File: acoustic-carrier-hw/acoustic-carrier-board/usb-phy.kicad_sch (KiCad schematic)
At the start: 59 parts, among them IC1 ECP5-BGA256, J9 TYPE-C-31-M-12, U18 LMV321, U6 TS3USB30EDGSR, U7 USB3300-EZK, Y3 Crystal_GND24_Small

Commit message: [carrier] Added hierarchical labels
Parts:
- removed IC1: ECP5-BGA256, iw-fpga_mcu:BGA256C80P16X16_1400X1400X170, symbol iw-fpga_mcu:ECP5-BGA256
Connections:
- net USB_SENSE renamed FPGA_USB_SENSE
- no-connect marks 21 -> 5
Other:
- moved on the sheet: C116, C117, C118, C119, C128, C129, C130, C131, C132, C137, C138, C139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

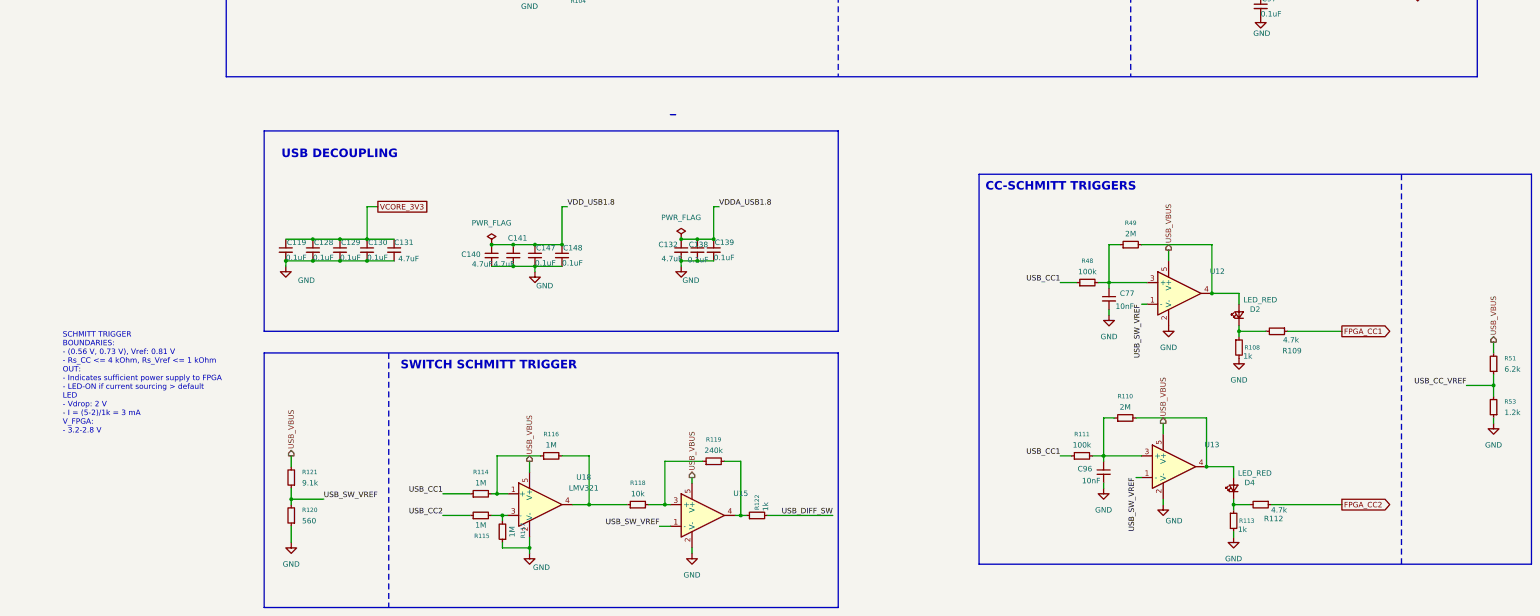
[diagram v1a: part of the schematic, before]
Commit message: [carrier] Added decoupling caps to flash and comparators
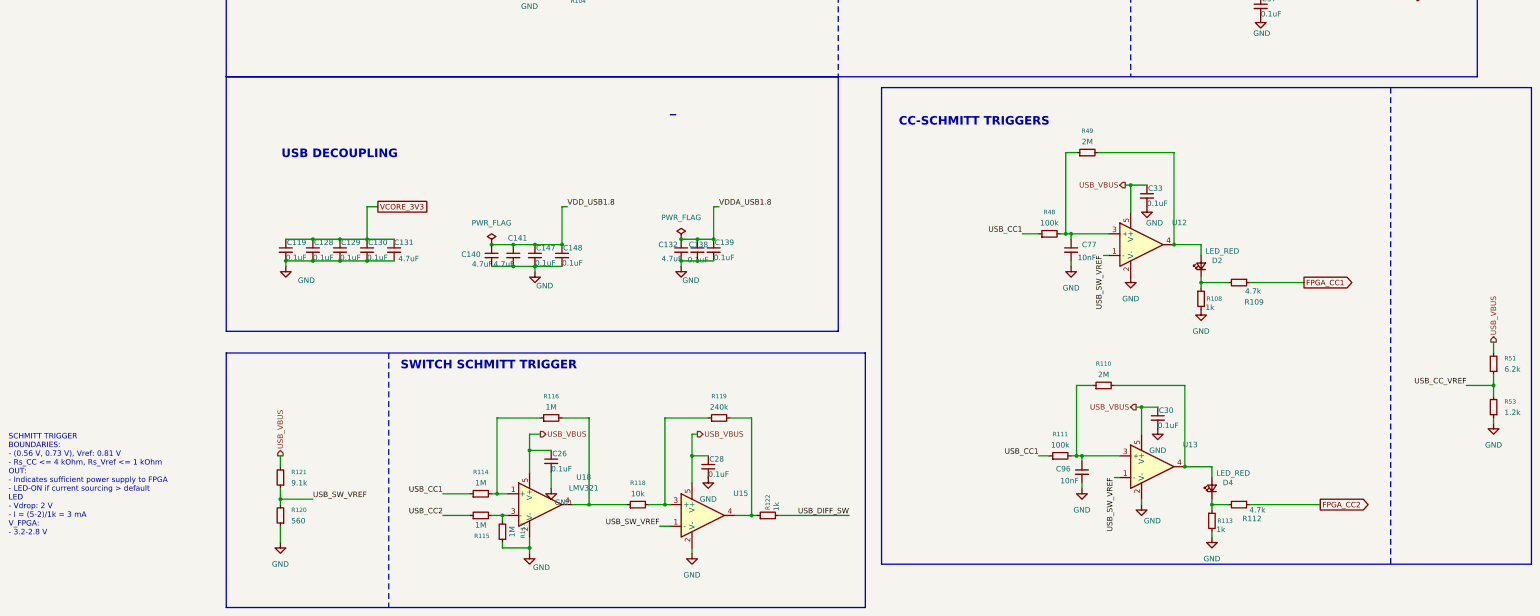
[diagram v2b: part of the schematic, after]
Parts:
- added C26, C28, C30, C33: 0.1uF, Capacitor_SMD:C_0402_1005Metric, symbol Device:C_Small
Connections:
- net GND: now also C26.2, C28.2, C30.2, C33.2
- net USB_VBUS: now also C26.1, C28.1, C30.1, C33.1
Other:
- moved on the sheet: C77, C96, D2, D4, R108, R109, R110, R111, R112, R113, R116, R119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

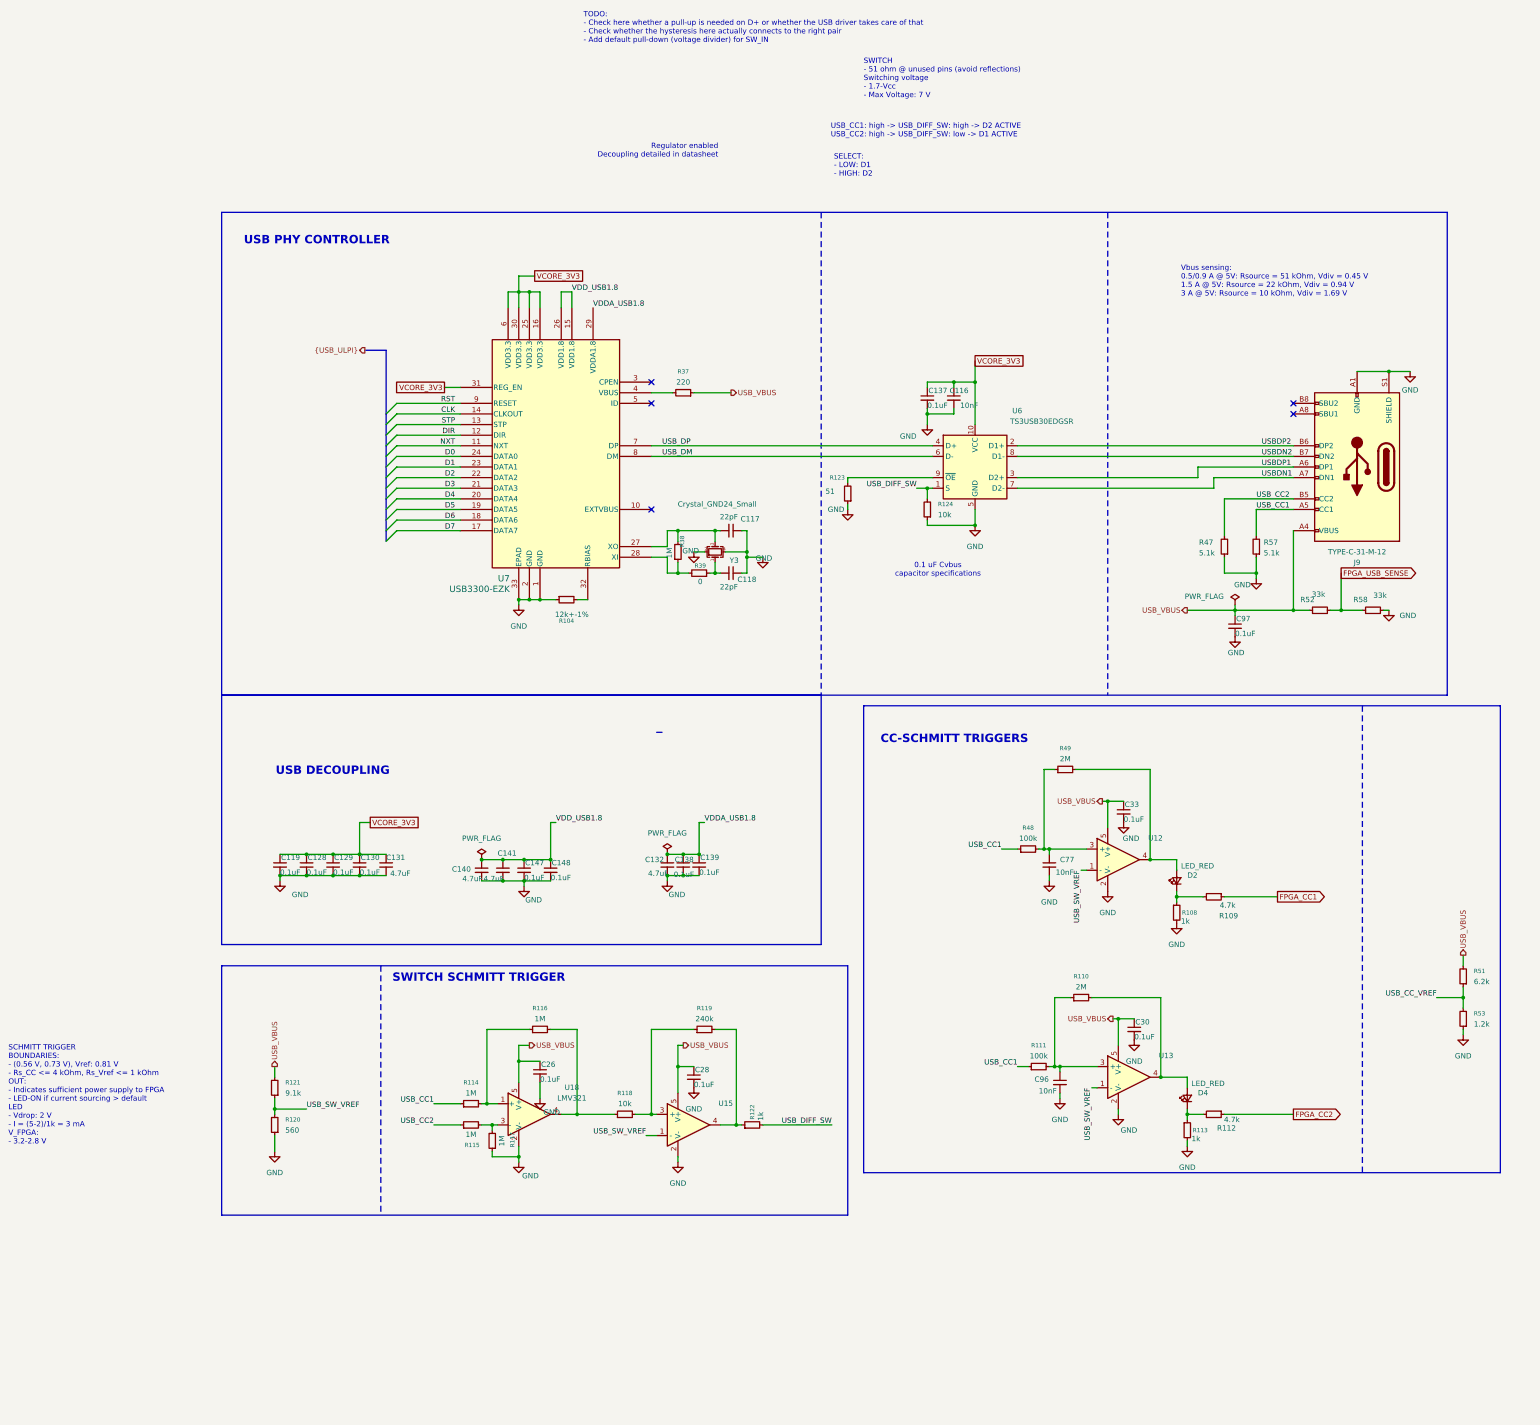
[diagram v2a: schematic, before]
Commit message: [¢arrier] Did major cchecks of ETH, DDR, ANALOG, config (next) check buffer circuit driven by USB-CC, then start layout
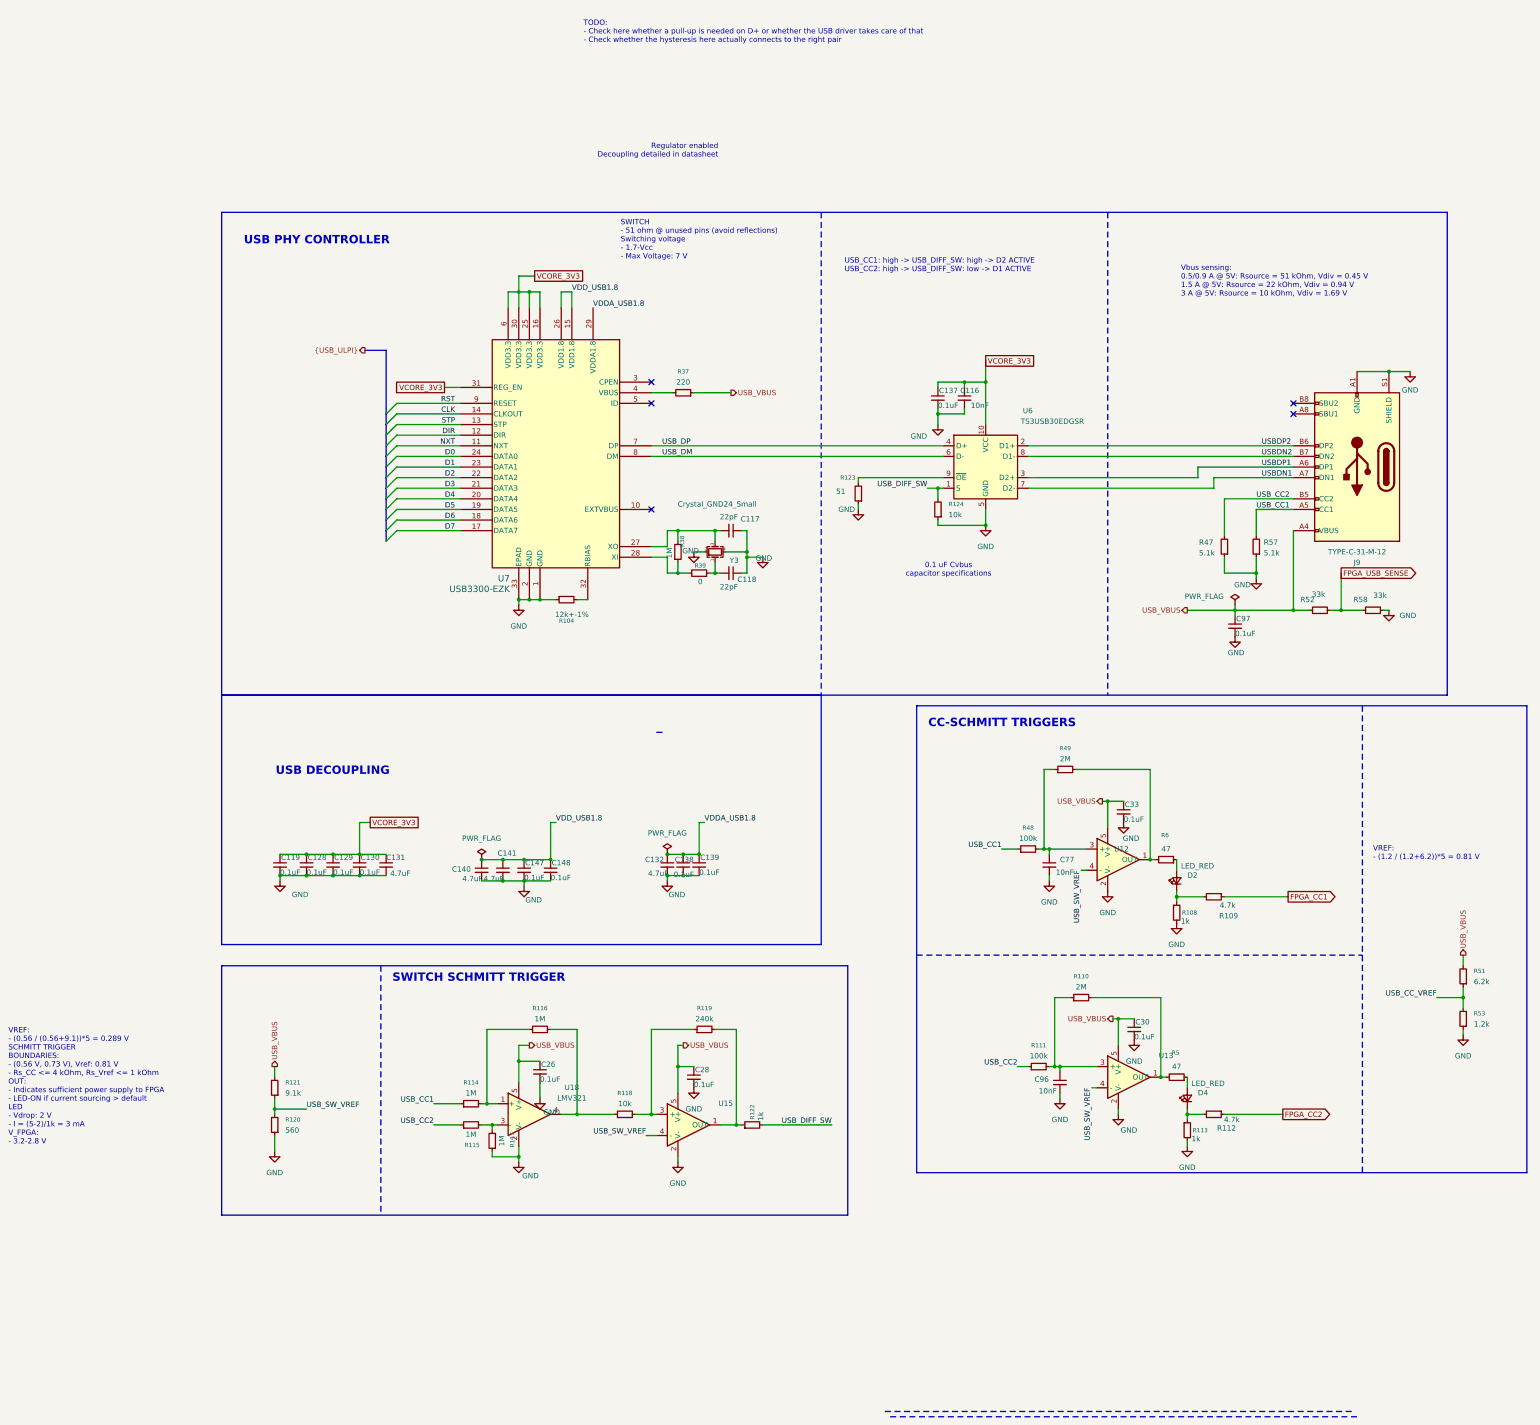
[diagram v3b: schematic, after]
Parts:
- added R5, R6: 47, Resistor_SMD:R_0603_1608Metric, symbol Device:R_Small
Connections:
- net USB_CC1: no longer R111.1
- net USB_CC2: now also R111.1
- net USB_SW_VREF: now also U12.4 (-), U13.4 (-), U15.4 (-); no longer U12.1 (-), U13.1 (-), U15.1 (-)
- net at R119.2, R122.1: now also U15.1 (OUT); no longer U15.4
- new net: D2.2 (A), R6.1
- new net: R49.2, R6.2, U12.1 (OUT)
- new net: D4.2 (A), R5.1
- new net: R110.2, R5.2, U13.1 (OUT)
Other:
- note added: "TODO: - Check here whether a pull-up is needed on D+ or whether the USB driver takes care of that - Check whether the hysteresis here actually connects to the right pair"
- note added: "VREF: - (0.56 / (0.56+9.1))*5 = 0.289 V SCHMITT TRIGGER BOUNDARIES: - (0.56 V, 0.73 V), Vref: 0.81 V - Rs_CC <= 4 kOhm, Rs_Vref <= 1 kOhm OUT: - Indicates sufficient power supply to FPGA - LED-ON if current sourcing > default LED - Vdrop: 2 V - I = (5-2)/1k = 3 mA V_FPGA: - 3.2-2.8 V"
- note added: "VREF: - (1.2 / (1.2+6.2))*5 = 0.81 V"
- note removed: "SCHMITT TRIGGER BOUNDARIES: - (0.56 V, 0.73 V), Vref: 0.81 V - Rs_CC <= 4 kOhm, Rs_Vref <= 1 kOhm OUT: - Indicates sufficient power supply to FPGA - LED-ON if current sourcing > default LED - Vdrop: 2 V - I = (5-2)/1k = 3 mA V_FPGA: - 3.2-2.8 V"
- note removed: "SELECT: - LOW: D1 - HIGH: D2"
- note removed: "TODO: - Check here whether a pull-up is needed on D+ or whether the USB driver takes care of that - Check whether the hysteresis here actually connects to the right pair - Add default pull-down (voltage divider) for SW_IN"
- moved on the sheet: C116, C137, R123, R124, U6
